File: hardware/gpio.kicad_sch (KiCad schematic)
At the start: 10 parts, among them J8 UART, J9 GPIO, Q4 BSN20

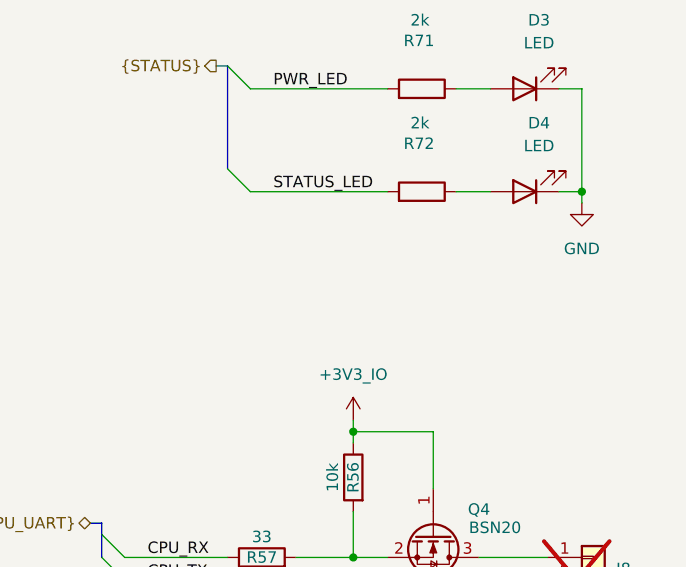
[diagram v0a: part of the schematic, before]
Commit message: Improve heat dissipation and layout
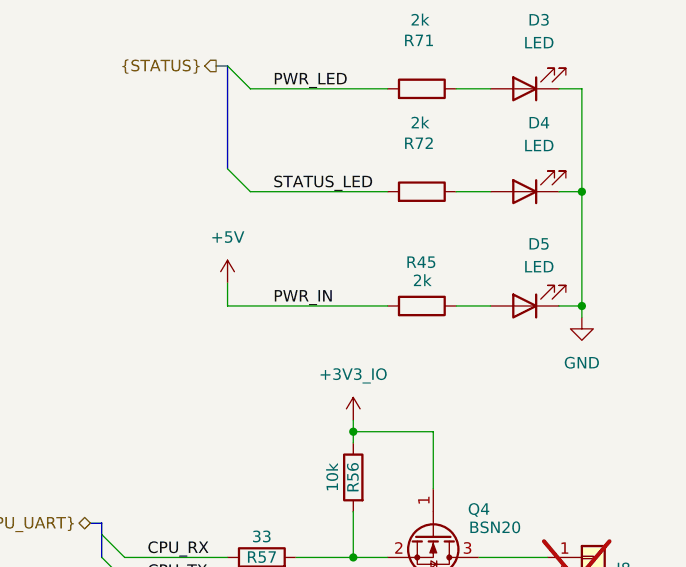
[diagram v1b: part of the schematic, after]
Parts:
- added D5: LED, LED_SMD:LED_0603_1608Metric, symbol Device:LED
- added R45: 2k, Resistor_SMD:R_0402_1005Metric, symbol Device:R
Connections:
- net +5V: now also R45.2
- net GND: now also D5.1 (K)
- new net: D5.2 (A), R45.1
